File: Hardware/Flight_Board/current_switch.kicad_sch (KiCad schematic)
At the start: 16 parts, among them U7 TPS274160A

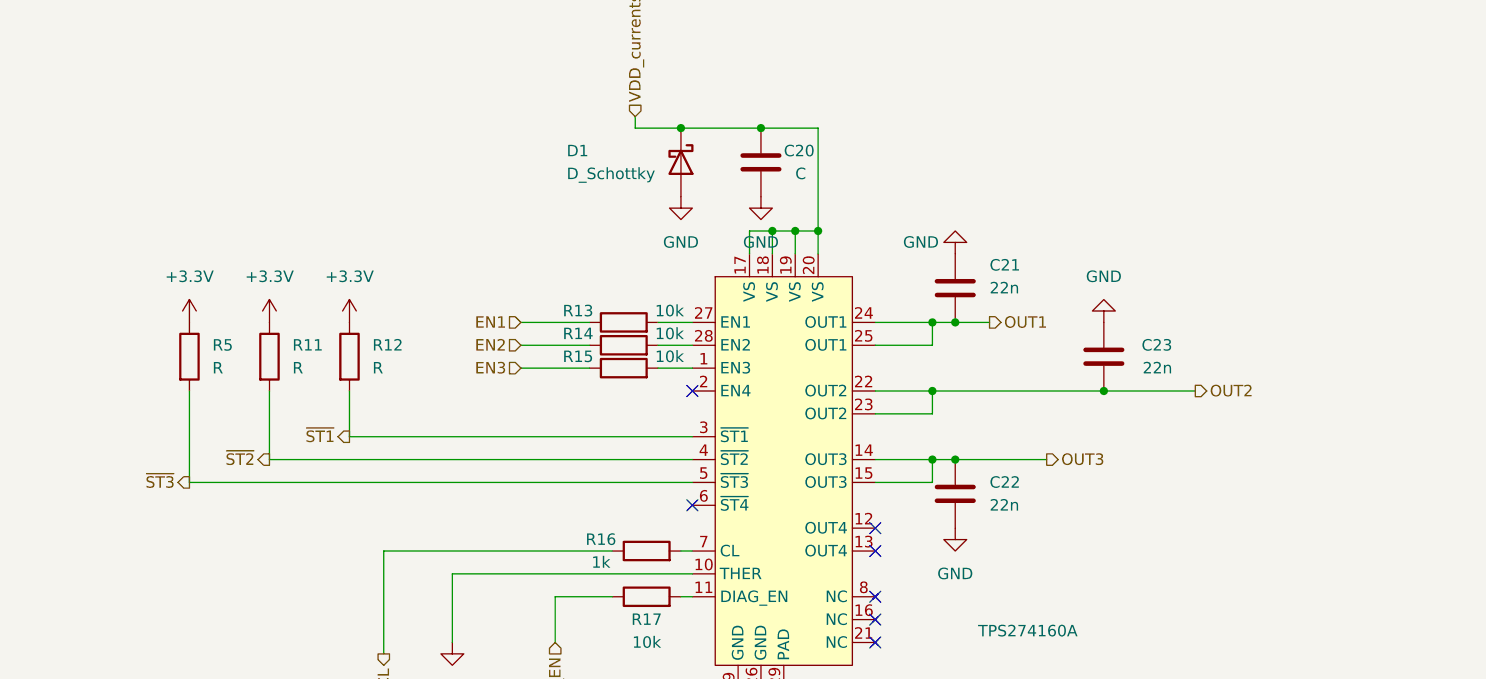
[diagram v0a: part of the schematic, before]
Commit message: remove STBar pullups
note made to toggle internal pullups on mcu to handle external pullups for diagnostic lines
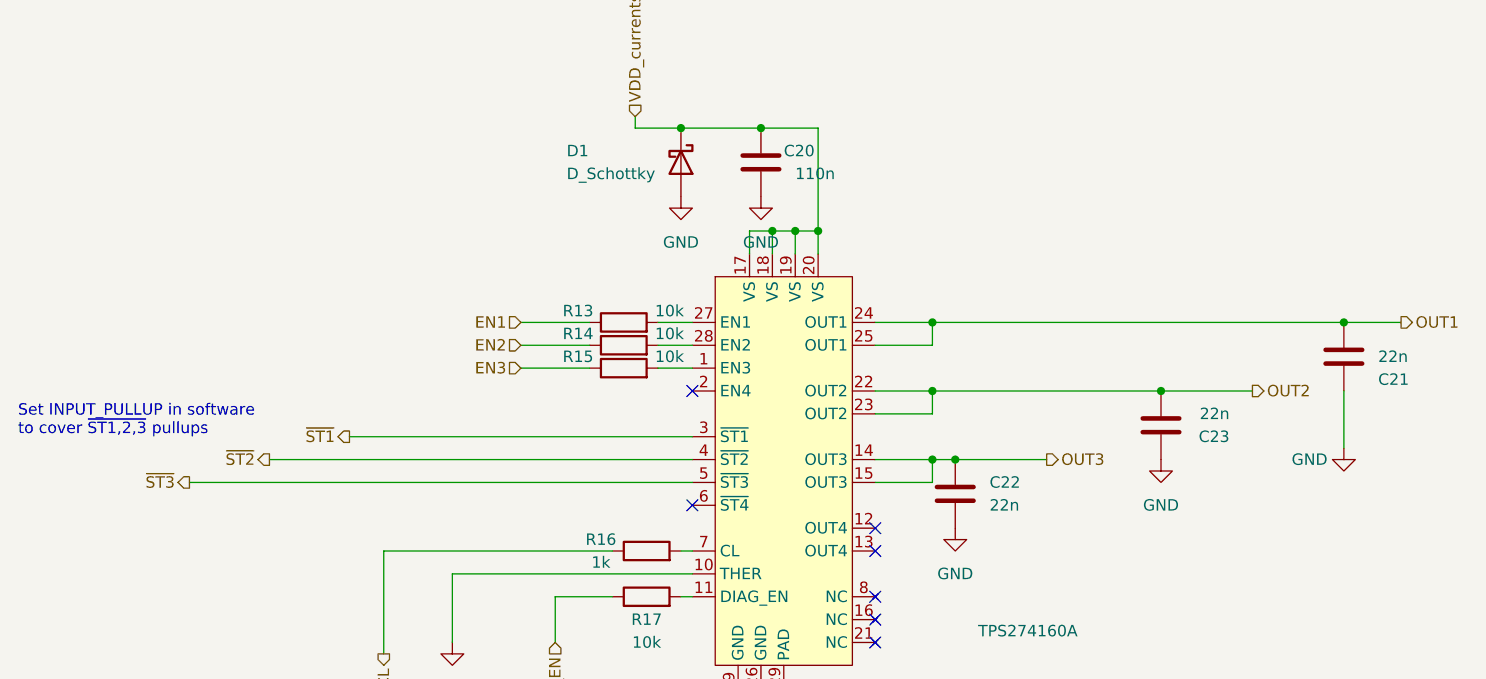
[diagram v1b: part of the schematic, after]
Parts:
- removed R11, R12, R5: R, symbol Device:R
- C20: value C -> 110n
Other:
- note added: "Set INPUT_PULLUP in software to cover ~{ST1,2,3} pullups"
- moved on the sheet: C21, C23

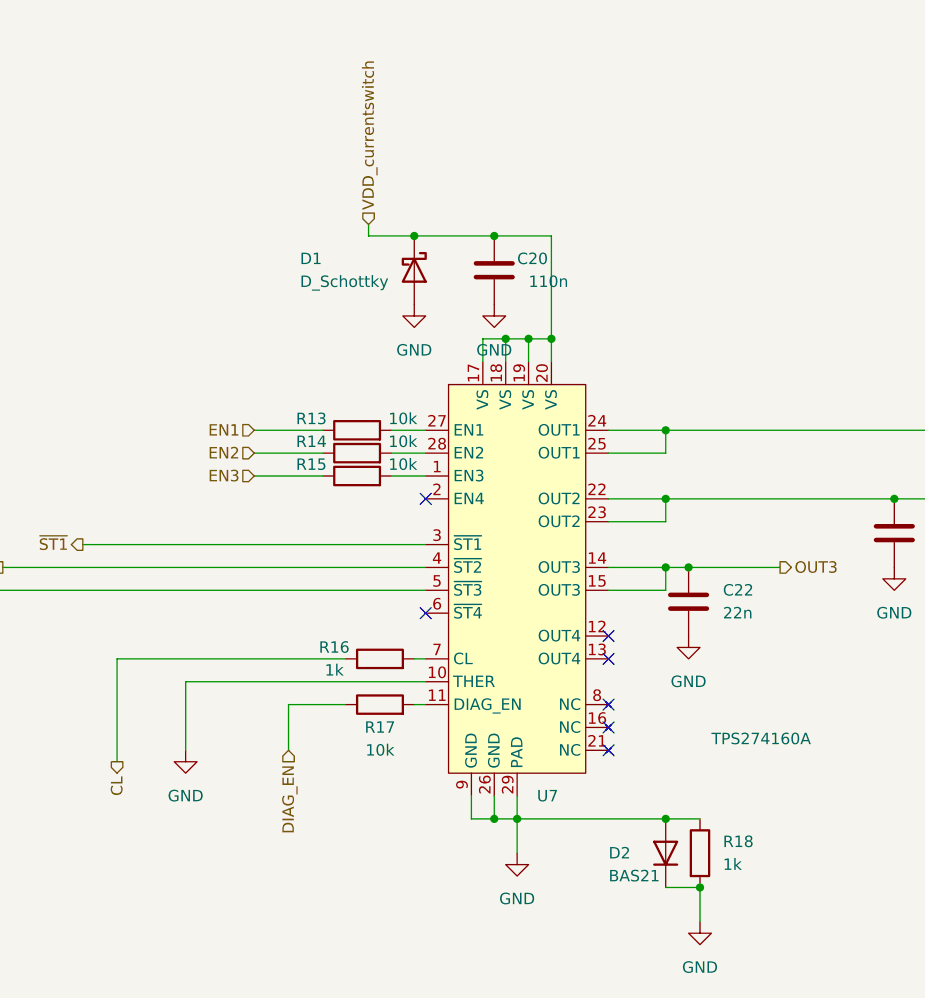
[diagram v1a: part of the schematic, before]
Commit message: fix current limiter
reverse polarity protection diode&res removed
split/fix caps on current switch VDD
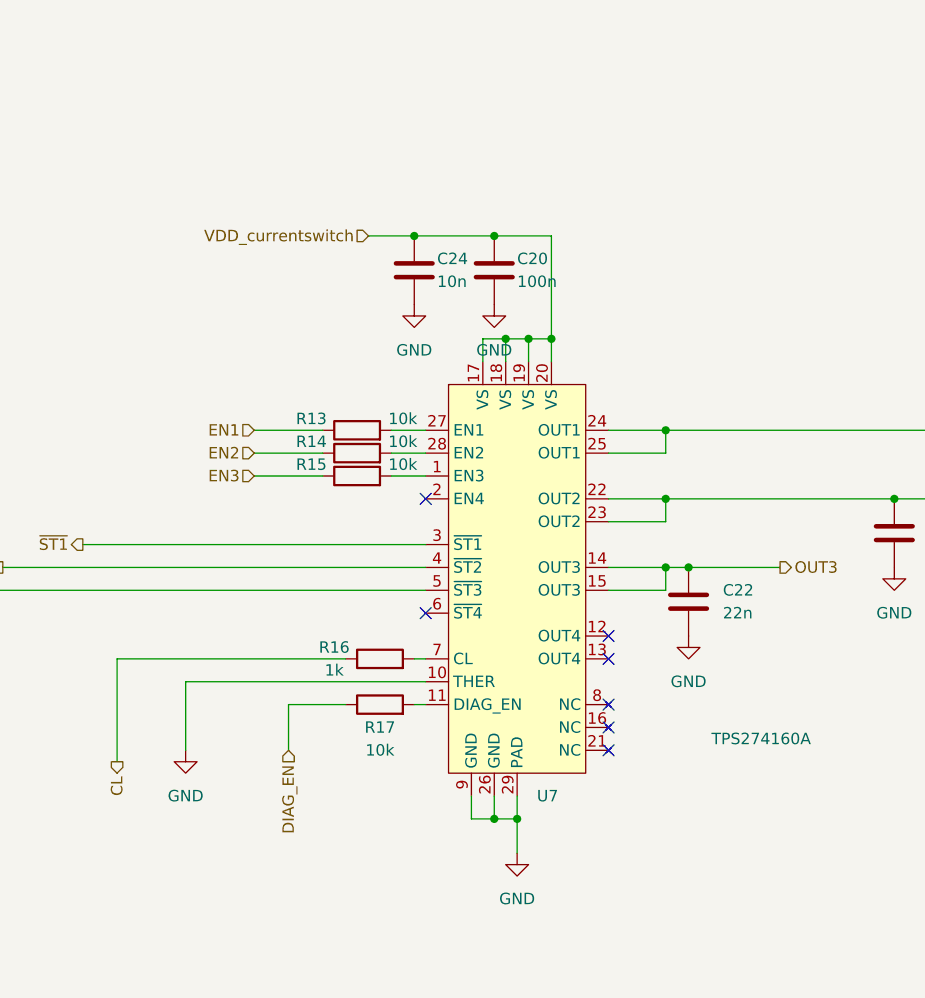
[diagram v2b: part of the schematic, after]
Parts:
- removed D1: D_Schottky, symbol Device:D_Schottky
- removed D2: BAS21, Package_TO_SOT_SMD:SOT-23, symbol Diode:BAS21
- removed R18: 1k, symbol Device:R
- added C24: 10n, symbol Device:C
- C20: value 110n -> 100n
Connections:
- net GND: now also C24.2
- net VDD_currentswitch: now also C24.1

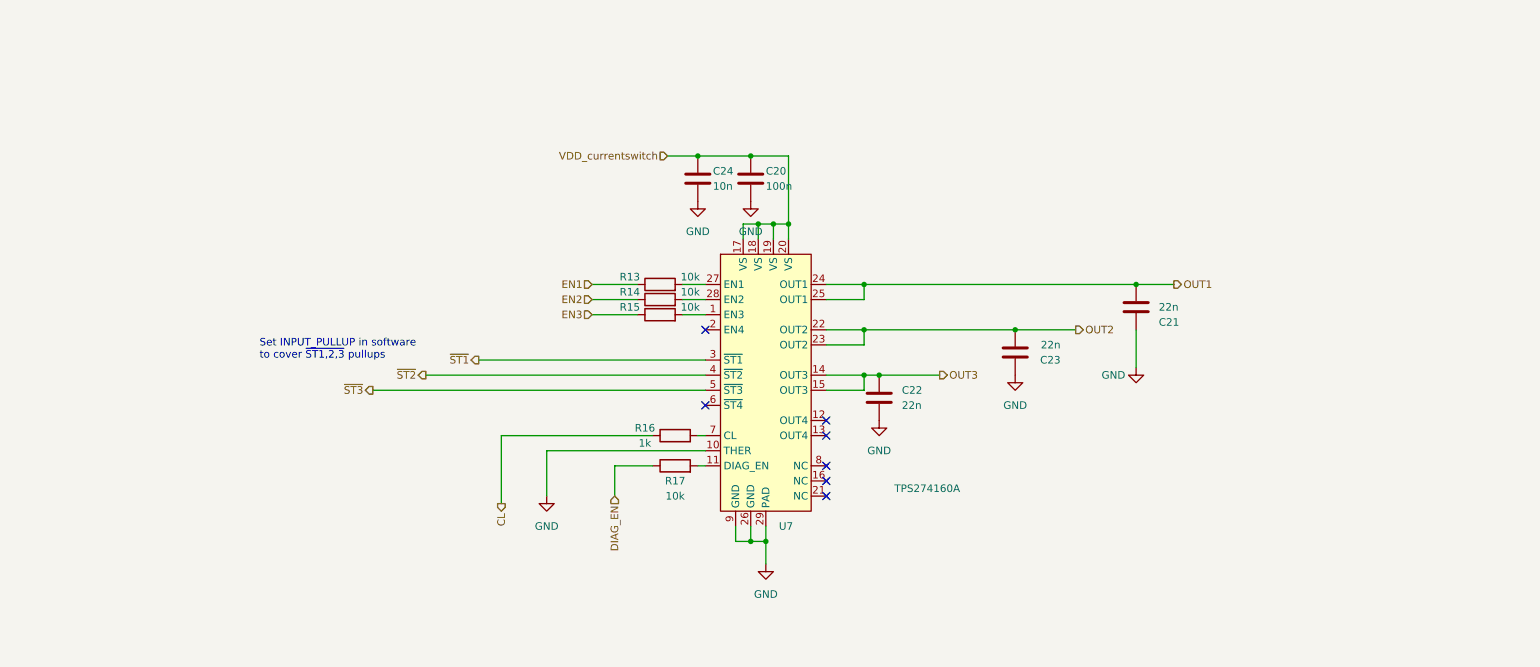
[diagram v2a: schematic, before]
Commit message: connect 4th output channel
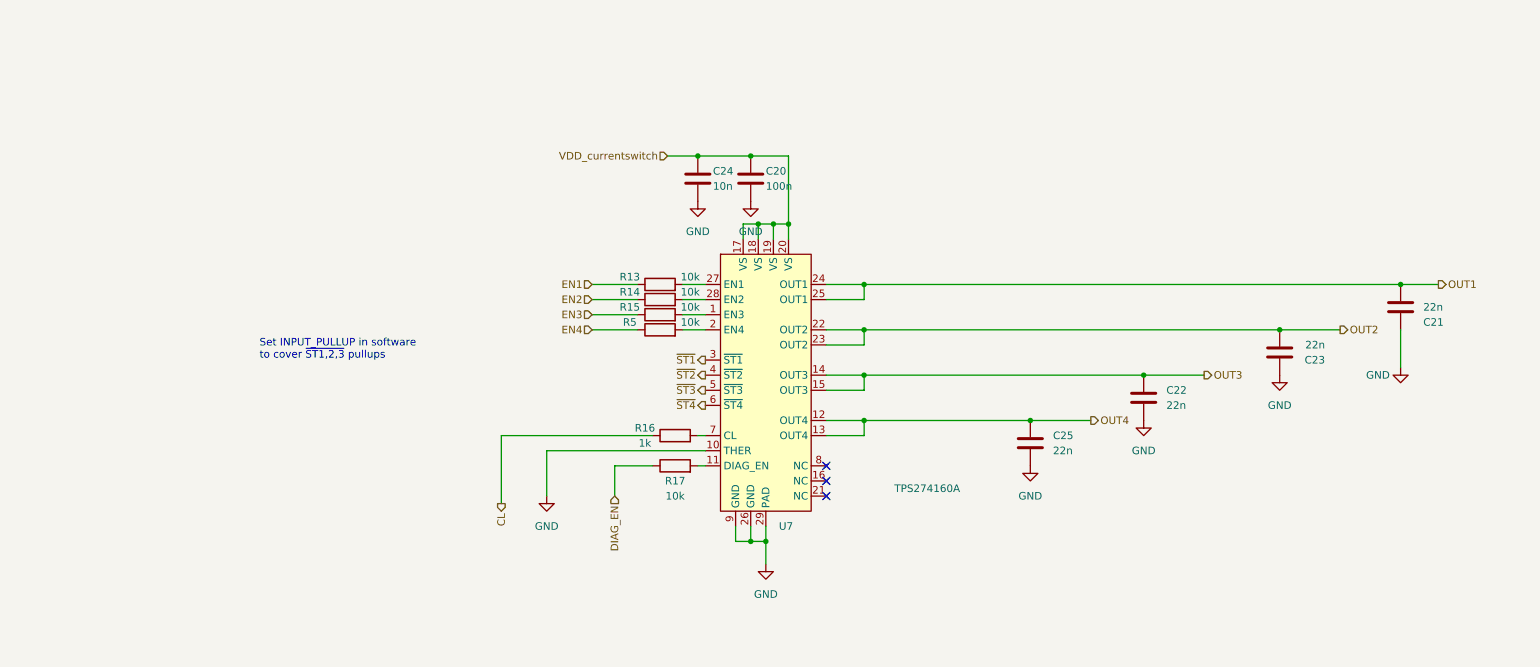
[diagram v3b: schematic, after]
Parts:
- added C25: 22n, symbol Device:C
- added R5: 10k, symbol Device:R
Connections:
- net GND: now also C25.2
- net OUT4: now reaches U7.12 (OUT4)
- net OUT4: now also U7.13 (OUT4), C25.1
- net at U7.2 (EN4): now also R5.2
- net ~{ST4}: now reaches U7.6 (~{ST4})
- new net EN4: R5.1
- no-connect marks 7 -> 3
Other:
- moved on the sheet: C21, C22, C23

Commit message: clean up and finalize initial design
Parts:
- removed C21, C22, C23: 22n, symbol Device:C
- added C30, C31, C32: 22n, symbol Device:C
- added R19, R20, R21, R22: 22k, symbol Device:R
- renumbered C24 to C27, C20 to C28, C25 to C29, R5 to R16, R16 to R17, R17 to R18, U7 to U8
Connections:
- net CL is gone; now on net GND: R17.1
- net GND: now also C30.2, C31.2, C32.2
- net OUT1: now also C32.1, R22.2
- net OUT2: now also C31.1, R21.2
- net OUT3: now also C30.1, R20.2
- net OUT4: now also R19.2
- net DIAG_EN renamed +3.3V
- net VDD_currentswitch renamed VPYRO
- net VPYRO: now also R19.1, R20.1, R21.1, R22.1
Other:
- moved on the sheet: C27, C28

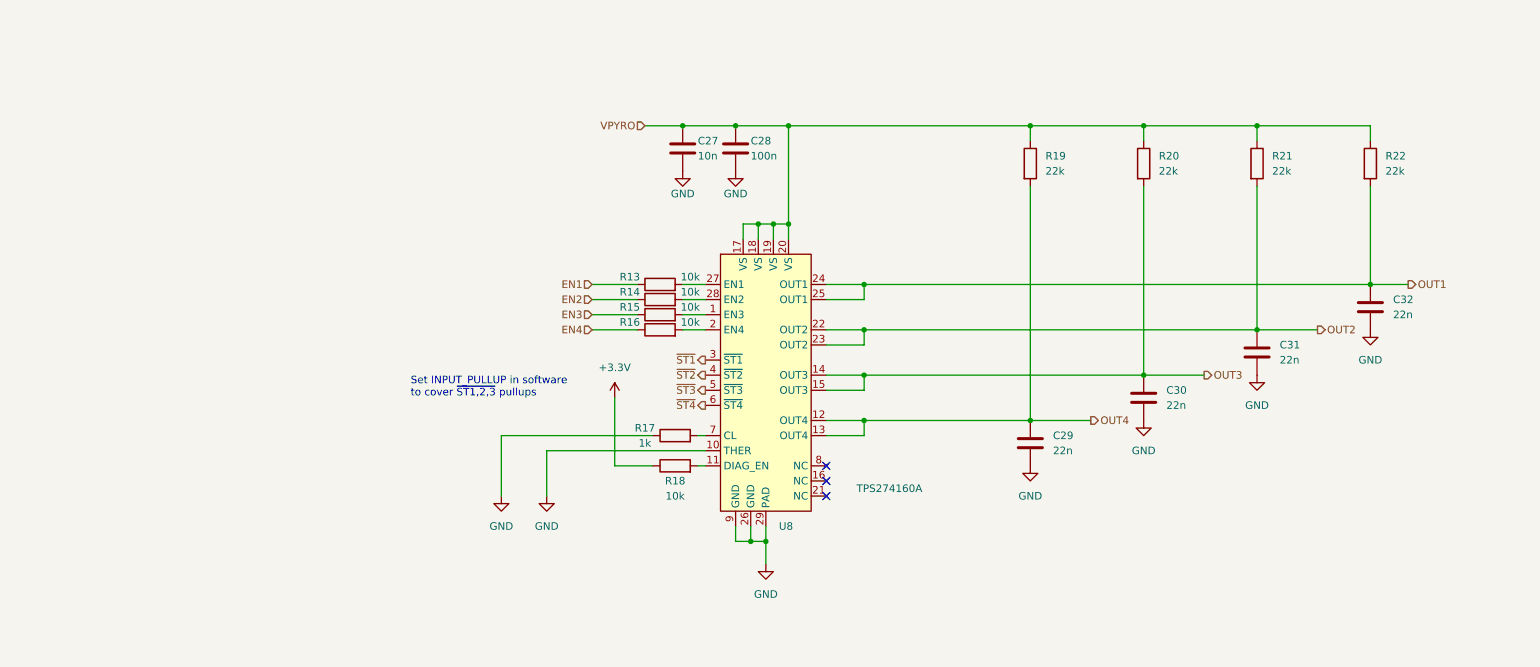
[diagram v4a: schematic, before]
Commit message: Clean up, relabel all refdes, and add autosaved files to gitignore
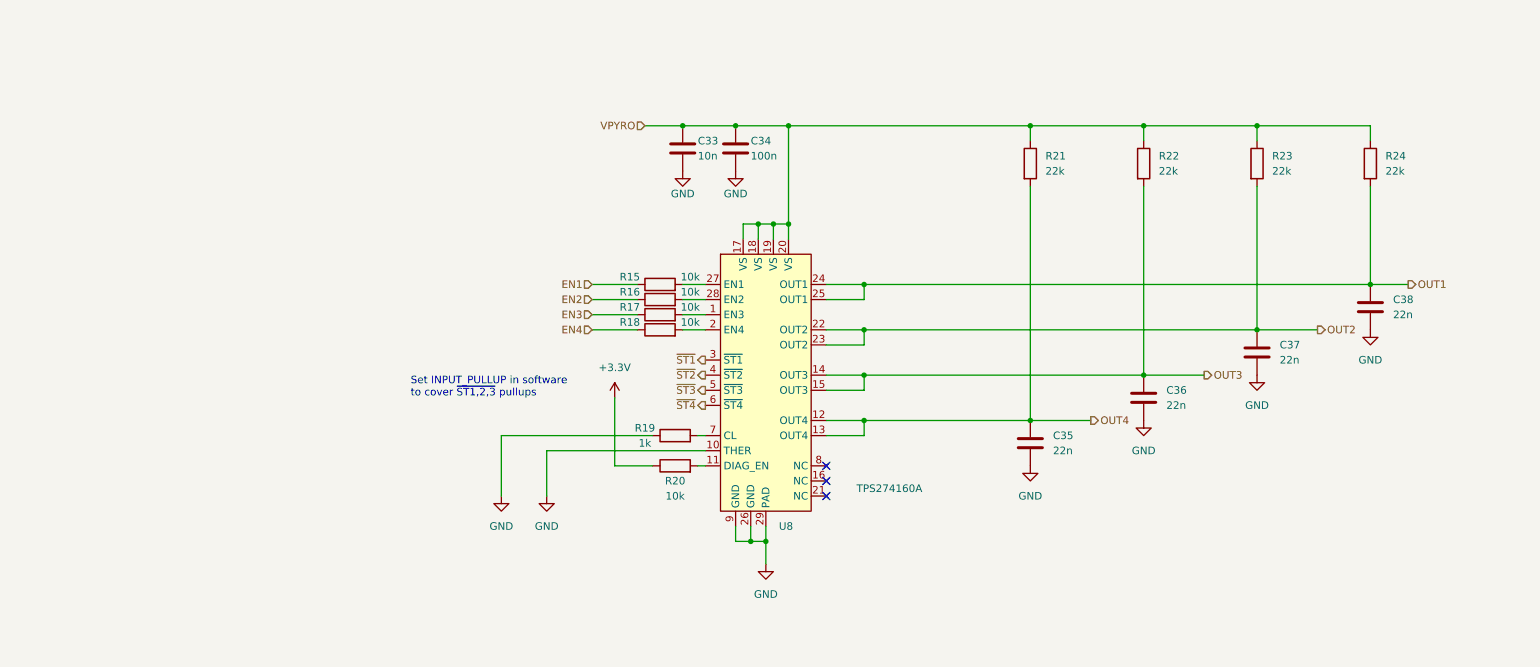
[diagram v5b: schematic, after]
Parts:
- renumbered C27 to C33, C28 to C34, C29 to C35, C30 to C36, C31 to C37, C32 to C38, R13 to R15, R14 to R16, R15 to R17, R16 to R18, R17 to R19, R18 to R20, R19 to R21, R20 to R22, R21 to R23, R22 to R24

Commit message: clean up, implement suggestions from saunders
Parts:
- added R27, R28, R29, R30: 10k, symbol Device:R
- R15, R16, R17, R18: value 10k -> 4.7k
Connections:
- net EN1: now also R27.2
- net EN2: now also R28.2
- net EN3: now also R29.2
- net EN4: now also R30.2
- net GND: now also R27.1, R28.1, R29.1, R30.1
- no-connect marks 3 -> 0
